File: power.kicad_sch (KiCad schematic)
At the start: 15 parts, among them U301 3.3, U302 TPS7B8733QKVURQ1

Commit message: fixed like a bunch of things, power and new xcvr and lights and other goodies, also started layout
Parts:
- removed C301, C303, C307, C308: 22u, Capacitor_SMD:C_0805_2012Metric_Pad1.18x1.45mm_HandSolder, symbol bfr_capacitors:CL21A226MAQNNNE
- removed C304, C305, C306, C310: 100n, Capacitor_SMD:C_0603_1608Metric_Pad1.08x0.95mm_HandSolder, symbol bfr_capacitors:06035C104KAT2A
- removed JP301: PWR_SEL, symbol Jumper:SolderJumper_2_Open
- removed JP302: APWR_SEL1, symbol Jumper:SolderJumper_2_Open
- removed JP303: APWR_SEL0, symbol Jumper:SolderJumper_2_Open
- removed U301: 3.3, Package_TO_SOT_SMD:SOT-223-3_TabPin2, symbol bfr_power_ics:AMS1117-3.3
- added C301, C303, C304, C306: 1u, Capacitor_SMD:C_0402_1005Metric_Pad0.74x0.62mm_HandSolder, symbol bfr_capacitors:CL05A105KA5NQNC
- added JP301: AVDD_SEL, Jumper:SolderJumper-3_P1.3mm_Bridged2Bar12_Pad1.0x1.5mm_NumberLabels, symbol Jumper:SolderJumper_3_Bridged12
- renumbered C309 to C305, U302 to U301
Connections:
- net 3V3: now also C305.1, U301.5 (VO), C304.1, C306.1, JP301.1 (A)
- net 3V3A: now also JP301.2 (C)
- net GNDPWR: now also C301.2, C303.2, C304.2, C306.2
- net 5V renamed Power Protection/5V_PROT
- net Power Protection/5V_PROT: now also C301.1, C303.1
- net PowerGood renamed Diagnostic LED/Vin
- new net Power Protection/3V3A_PROT: JP301.3 (B)
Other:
- added sheet Diagnostic LED (diag_led.kicad_sch)
- sheet Power Protection ports: added 3V3A_PROT, 3V3A_RAW; removed 3V3_PROT, 3V3_RAW
- note added: "ok so power scheme is, u power board off 5V and onboard LDO will convert it down with high PSRR. have option to power analog periphs off external power, that's it"
- note removed: "TODO: is it actually worth it"
- note removed: "if 3v3 bus is disconnected, gate of Q5 pulled low and current may flow from 5V bus if 3v3 bus is active, Vsg of Q5 is like -1V bc schottky and thus basically deactivates the 5V bus this way if 3v3 and 5v bus both get power, chip "prefers" 3v3 bus to avoid power loss from dumping over LDO issue if reverse voltage, but figure probably okay becuase RVP"
- moved on the sheet: C302, C305, U301

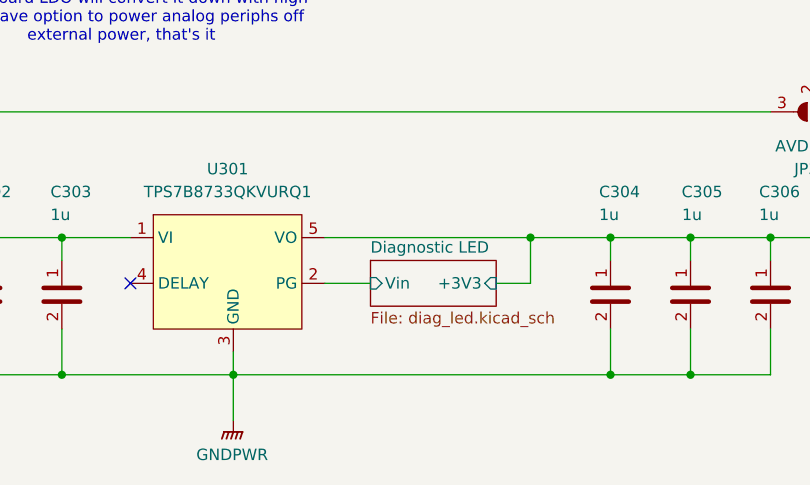
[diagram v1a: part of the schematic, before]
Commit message: quicksave on some R.S. T.S. (mostly layout changes, small pin changes for better routing)
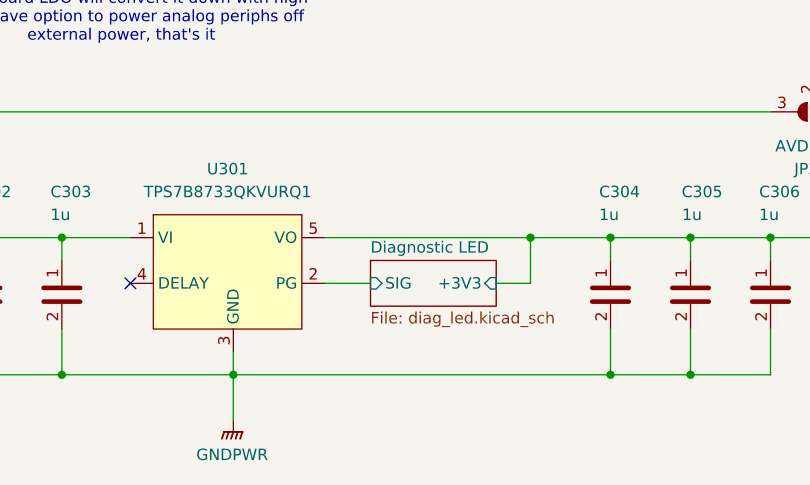
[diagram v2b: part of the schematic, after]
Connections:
- net Diagnostic LED/Vin renamed Diagnostic LED/SIG
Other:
- sheet Diagnostic LED ports: added SIG; removed Vin
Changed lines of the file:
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@@
 			)
 		)
-		(pin "Vin" input
+		(pin "SIG" input
 			(at 162.56 90.17 180)
 			(effects
@@
 			(project "DU UC V1 - Minnow"
 				(path "/0aeff2df-21bc-4c76-95d6-83ff8577a8db/02d78338-99c8-4e1a-a94d-a7a2643a4fea"
-					(page "")
+					(page "#")
 				)
 			)

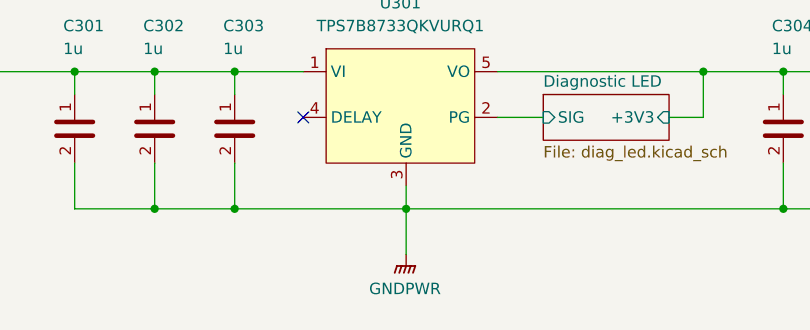
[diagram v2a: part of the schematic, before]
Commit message: laid out most of power, main xcvr, prob some other stuff
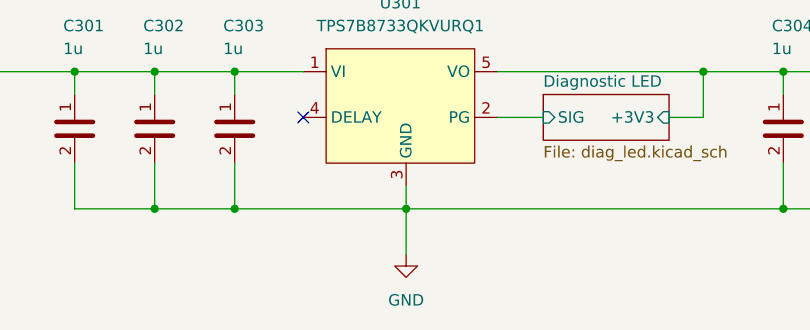
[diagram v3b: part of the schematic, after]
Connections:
- net GNDPWR renamed GND
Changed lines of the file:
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@@
 	)
 	(symbol
-		(lib_id "power:GNDPWR")
+		(lib_id "power:GND")
 		(at 147.32 105.41 0)
 		(unit 1)
@@
 		(fields_autoplaced yes)
 		(property "Reference" "#PWR0323"
-			(at 147.32 110.49 0)
+			(at 147.32 111.76 0)
 			(effects
 				(font
@@
 			)
 		)
-		(property "Value" "GNDPWR"
-			(at 147.193 109.22 0)
+		(property "Value" "GND"
+			(at 147.32 110.49 0)
 			(effects
 				(font
@@
 		)
 		(property "Footprint" ""
-			(at 147.32 106.68 0)
+			(at 147.32 105.41 0)
 			(effects
 				(font
@@
 		)
 		(property "Datasheet" ""
-			(at 147.32 106.68 0)
+			(at 147.32 105.41 0)
 			(effects
 				(font
@@
 			)
 		)
-		(property "Description" "Power symbol creates a global label with name \"GNDPWR\" , global ground"
+		(property "Description" "Power symbol creates a global label with name \"GND\" , ground"
 			(at 147.32 105.41 0)
 			(effects
